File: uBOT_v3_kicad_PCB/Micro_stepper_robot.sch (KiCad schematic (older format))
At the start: 29 parts, among them J4 USB_B_Micro, M1 Stepper_Motor_bipolar, M2 Stepper_Motor_bipolar, M3 Stepper_Motor_bipolar, M4 Stepper_Motor_bipolar, SW3 EN, SW4 BOOT, U1 DRV8833PW, U2 TCRT5000, U4 ESP32-WROOM-32D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

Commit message: safety save
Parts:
- added C7, C8: 10uF, Capacitor_SMD:C_0805_2012Metric_Pad1.15x1.40mm_HandSolder, symbol Device:C_Small
- C3, C4: value C_Small -> 2.2uF
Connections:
- net +3V3: now also C8.1
- net +BATT: now also C7.2
- net GND: now also C7.1, C8.2
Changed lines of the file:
@@
 $EndComp
 Wire Wire Line
-	6050 1350 6050 1450
+	6050 1350 6050 1400
 $Comp
 L power:+3.3V #PWR0123
@@
 P 10000 4150
 F 0 "C4" H 9908 4104 50  0000 R CNN
-F 1 "C_Small" H 9908 4195 50  0000 R CNN
+F 1 "2.2uF" H 9908 4195 50  0000 R CNN
 F 2 "Capacitor_SMD:C_0805_2012Metric_Pad1.15x1.40mm_HandSolder" H 10000 4150 50  0001 C CNN
 F 3 "~" H 10000 4150 50  0001 C CNN
@@
 P 10000 1650
 F 0 "C3" H 9908 1604 50  0000 R CNN
-F 1 "C_Small" H 9908 1695 50  0000 R CNN
+F 1 "2.2uF" H 9908 1695 50  0000 R CNN
 F 2 "Capacitor_SMD:C_0805_2012Metric_Pad1.15x1.40mm_HandSolder" H 10000 1650 50  0001 C CNN
 F 3 "~" H 10000 1650 50  0001 C CNN
@@
 Wire Wire Line
 	1450 3850 1500 3850
+$Comp
+L Device:C_Small C8
+U 1 1 5F01A906
+P 6450 1200
+F 0 "C8" H 6542 1246 50  0000 L CNN
+F 1 "10uF" H 6542 1155 50  0000 L CNN
+F 2 "Capacitor_SMD:C_0805_2012Metric_Pad1.15x1.40mm_HandSolder" H 6450 1200 50  0001 C CNN
+F 3 "~" H 6450 1200 50  0001 C CNN
+	1    6450 1200
+	1    0    0    -1
+$EndComp
+Wire Wire Line
+	6450 1050 6450 1100
+Connection ~ 6450 1050
+Wire Wire Line
+	6450 1300 6450 1400
+Wire Wire Line
+	6450 1400 6050 1400
+Connection ~ 6050 1400
+Wire Wire Line
+	6050 1400 6050 1450
+$Comp
+L Device:C_Small C7
+U 1 1 5F029E4B
+P 2150 1100
+F 0 "C7" H 2058 1054 50  0000 R CNN
+F 1 "10uF" H 2300 1300 50  0000 R CNN
+F 2 "Capacitor_SMD:C_0805_2012Metric_Pad1.15x1.40mm_HandSolder" H 2150 1100 50  0001 C CNN
+F 3 "~" H 2150 1100 50  0001 C CNN
+	1    2150 1100
+	-1   0    0    1
+$EndComp
+Wire Wire Line
+	2150 1000 2150 900
+Wire Wire Line
+	2150 900  2400 900
+Connection ~ 2400 900
+Wire Wire Line
+	2150 1200 2150 1250
+Wire Wire Line
+	2150 1250 2400 1250
+Connection ~ 2400 1250
 $EndSCHEMATC

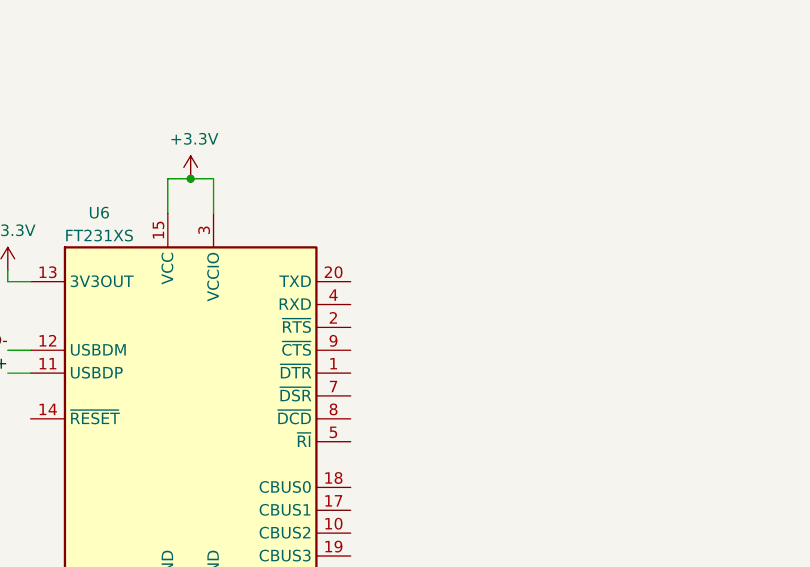
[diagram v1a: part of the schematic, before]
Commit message: ADDED TX AND TX CONNECTIONS TO USB/UART IC
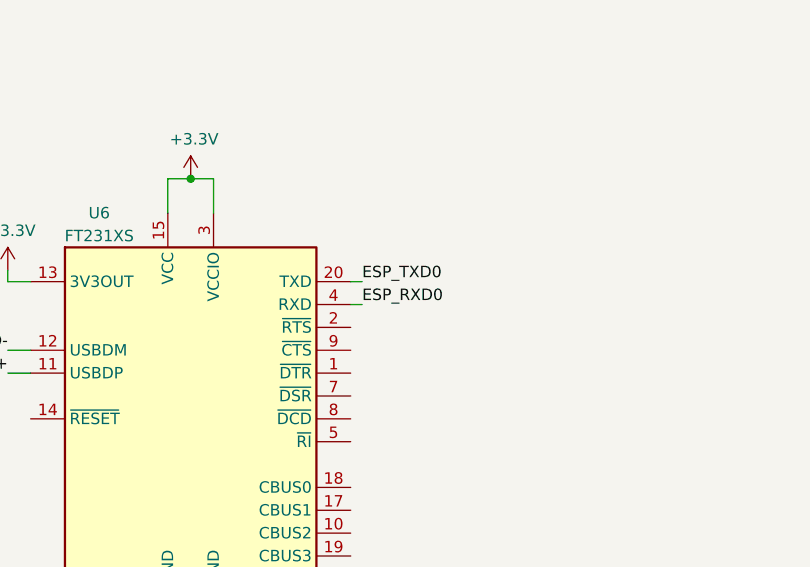
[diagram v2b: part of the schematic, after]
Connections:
- net ESP_RXD0: now also U6.4 (RXD)
- net ESP_TXD0: now also U6.20 (TXD)
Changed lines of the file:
@@
 	2150 1250 2400 1250
 Connection ~ 2400 1250
+Wire Wire Line
+	6550 3150 6500 3150
+Wire Wire Line
+	6500 3250 6550 3250
+Text Label 6550 3150 0    50   ~ 0
+ESP_TXD0
+Text Label 6550 3250 0    50   ~ 0
+ESP_RXD0
 $EndSCHEMATC
